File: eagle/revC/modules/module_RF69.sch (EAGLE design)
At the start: 17 parts, among them X1 734120110

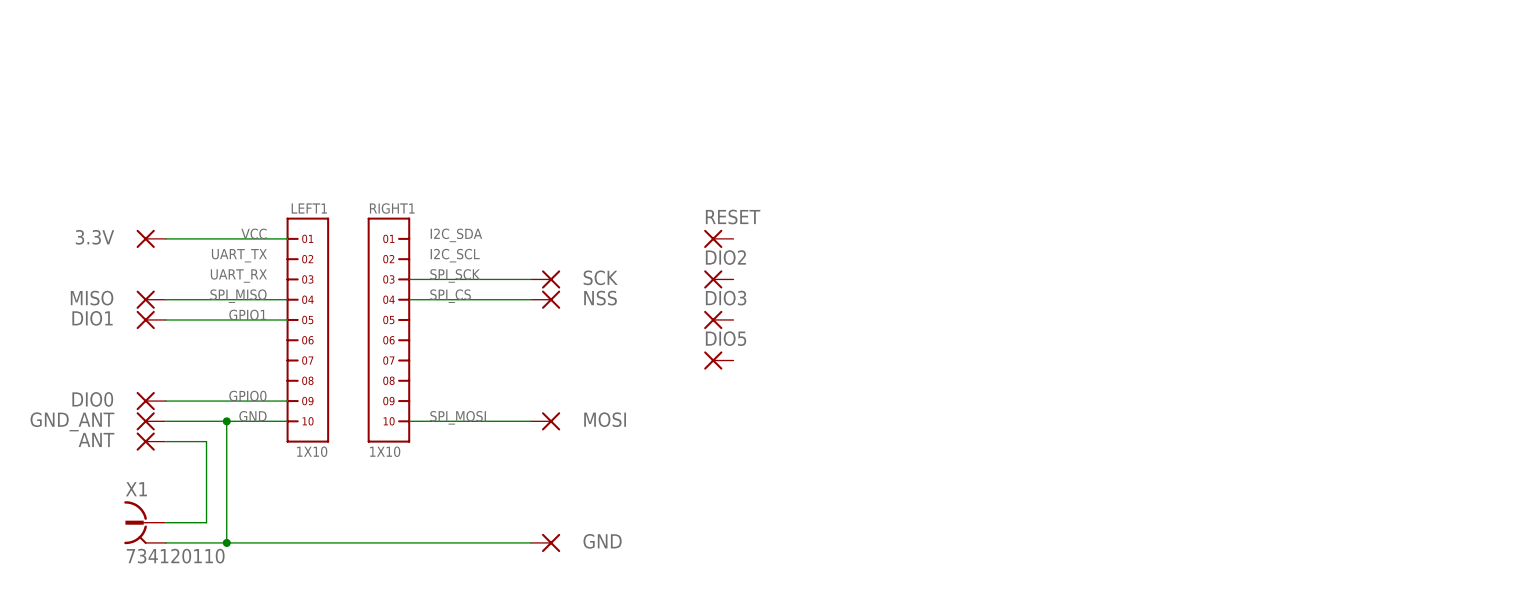
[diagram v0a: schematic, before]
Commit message: Replaced modules with library parts
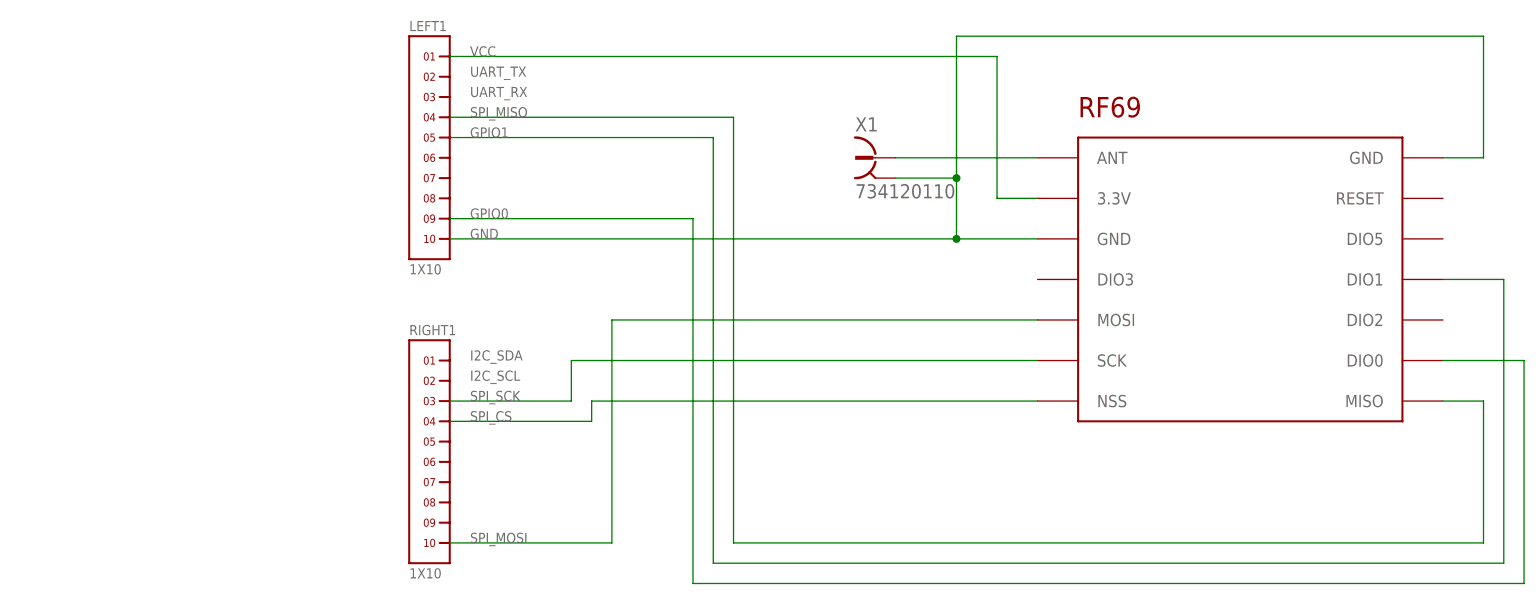
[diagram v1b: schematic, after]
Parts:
- removed 3.3V, ANT, DIO0, DIO1, DIO2, DIO3, DIO5, GND, GND_ANT, MISO, MOSI, NSS, RESET, SCK: (no value), wirepad:SMD2
- added U$1: RF69, RadioShield:RF69
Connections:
- removed net ANT: ANT.P, X1.1
- new net N$1: U$1.ANT, X1.1
- net GND: now also U$1.GND@1, U$1.GND@2; no longer GND.P, GND_ANT.P
- net INT0: now also U$1.DIO0; no longer DIO0.P
- net INT1: now also U$1.DIO1; no longer DIO1.P
- net SPI_CS: now also U$1.NSS; no longer NSS.P
- net SPI_MISO: now also U$1.MISO; no longer MISO.P
- net SPI_MOSI: now also U$1.MOSI; no longer MOSI.P
- net SPI_SCK: now also U$1.SCK; no longer SCK.P
- net VCC: now also U$1.3.3V; no longer 3.3V.P
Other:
- moved on the sheet: LEFT1, RIGHT1, X1
